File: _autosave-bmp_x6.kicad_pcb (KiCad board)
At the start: 2 copper layers, 50 x 50 mm, 67 parts, among them J1 USB_B, J2 Conn_01x05_Pin, J3 Conn_02x05_Odd_Even, Q1 NMOS, Q2 PMOS, Q3 PMOS, Q4 NMOS, SW1 SW_Push, U1 STM32F103CBTx, U2 USB6B1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

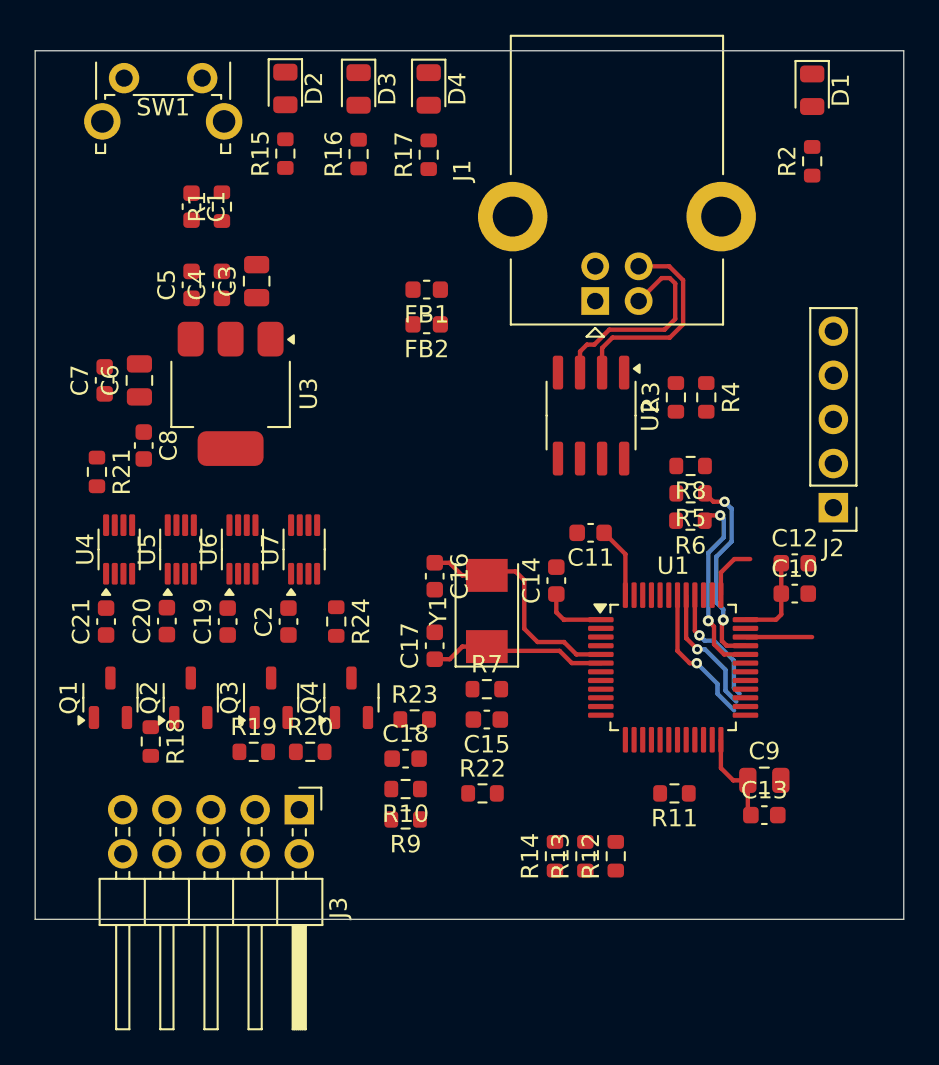
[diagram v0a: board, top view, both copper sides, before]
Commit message: shorcuts updated and components relocated.
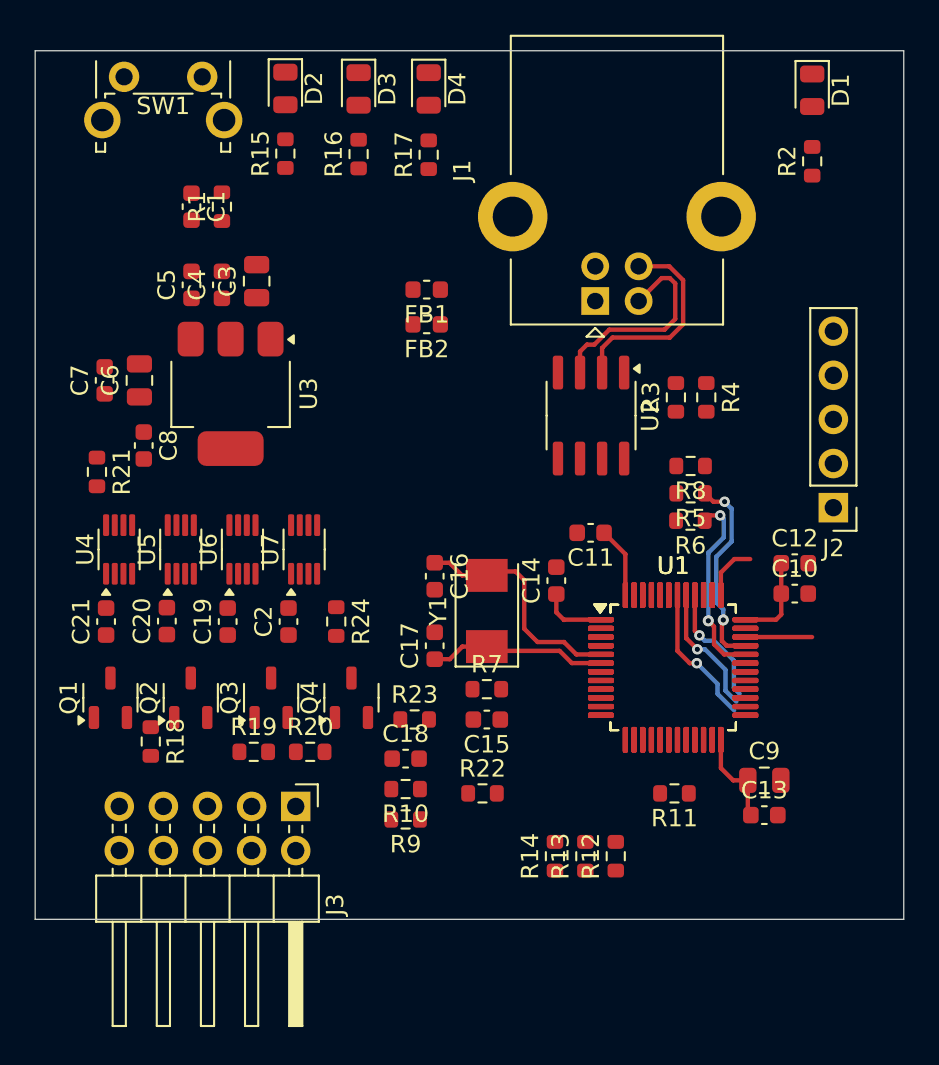
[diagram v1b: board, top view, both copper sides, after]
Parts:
- added U1 (x2): STM32F103CBTx, Package_QFP:LQFP-48_7x7mm_P0.5mm, F.Cu at (62.0, 55.2)
- moved J3 0.28 mm to (40.2, 63.2)
- moved SW1 0.08 mm to (30.4, 21.2)
